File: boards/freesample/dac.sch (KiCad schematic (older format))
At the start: 1 part

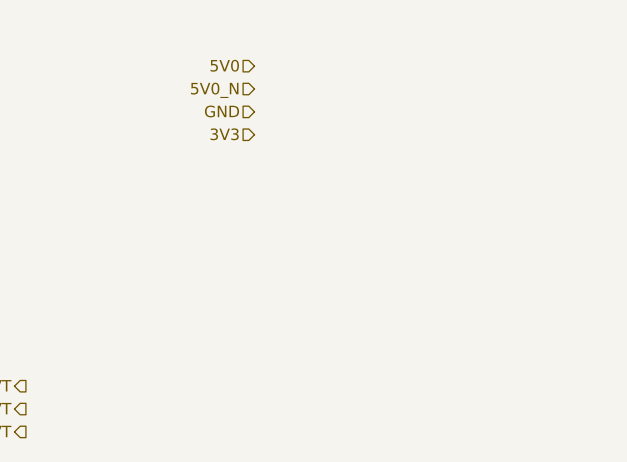
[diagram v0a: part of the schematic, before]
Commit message: Continued initial schematic capture
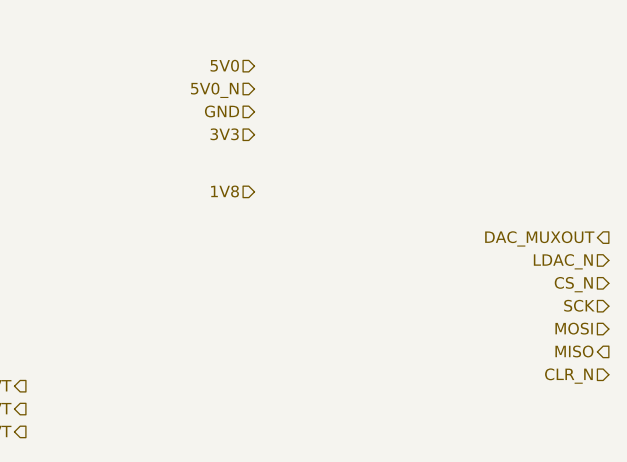
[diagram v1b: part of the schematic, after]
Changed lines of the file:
@@
 $Descr A4 11693 8268
 encoding utf-8
-Sheet 3 11
+Sheet 3 12
 Title "FREESAMPLE Oscilloscope"
-Date "2018-12-15"
+Date "2018-12-17"
 Rev "0.1"
 Comp "Andrew D. Zonenberg / Antikernel Labs"
@@
 Text HLabel 8100 3800 0    50   Input ~ 0
 3V3
+Text HLabel 9650 4250 0    50   Output ~ 0
+DAC_MUXOUT
+Text HLabel 9650 4350 0    50   Input ~ 0
+LDAC_N
+Text HLabel 9650 4450 0    50   Input ~ 0
+CS_N
+Text HLabel 9650 4550 0    50   Input ~ 0
+SCK
+Text HLabel 9650 4650 0    50   Input ~ 0
+MOSI
+Text HLabel 9650 4750 0    50   Output ~ 0
+MISO
+Text HLabel 9650 4850 0    50   Input ~ 0
+CLR_N
+Text HLabel 8100 4050 0    50   Input ~ 0
+1V8
 $EndSCHEMATC

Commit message: Continued work on schematic capture
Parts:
- gave numbers to parts that had none: 1
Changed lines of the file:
@@
 Rev "0.1"
 Comp "Andrew D. Zonenberg / Antikernel Labs"
-Comment1 ""
+Comment1 "DAC for setting sampling point Y position"
 Comment2 ""
 Comment3 ""
@@
 $EndDescr
 $Comp
-L analog-azonenberg:LTC2664 U?
+L analog-azonenberg:LTC2664 U4
 U 1 1 5C15756D
 P 4150 4450
-F 0 "U?" H 4650 7025 50  0000 C CNN
+F 0 "U4" H 4650 7025 50  0000 C CNN
 F 1 "LTC2664" H 4650 6934 50  0000 C CNN
 F 2 "" H 4150 4450 50  0001 C CNN

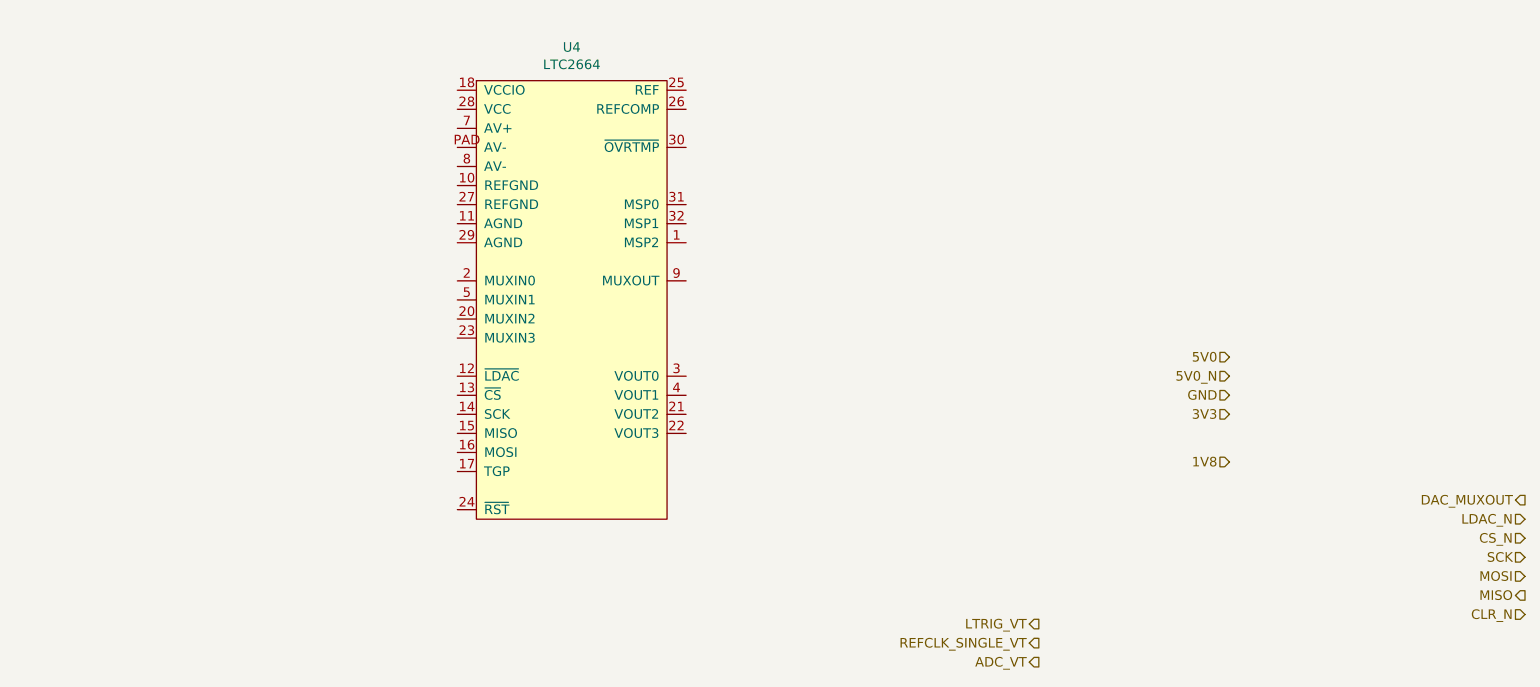
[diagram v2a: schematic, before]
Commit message: Continued work on FREESAMPLE schematic including PSU.
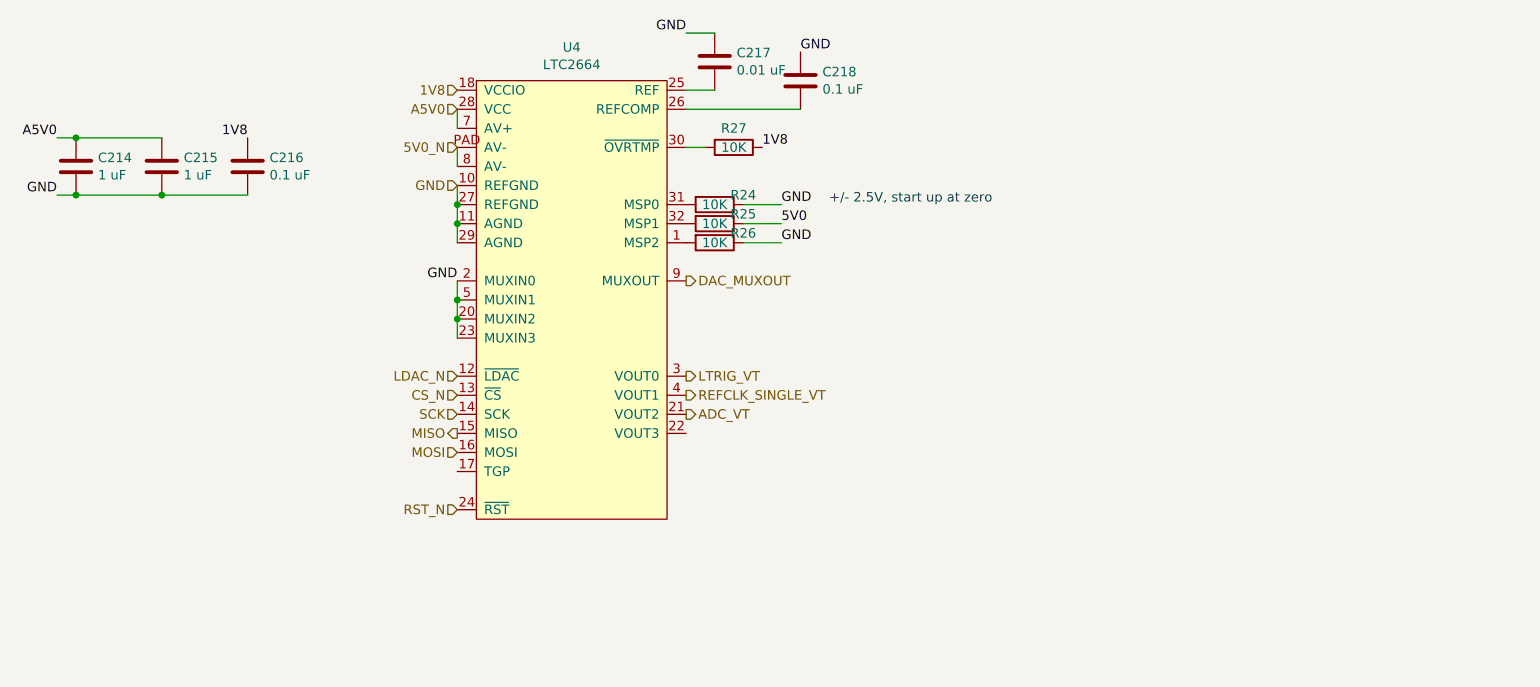
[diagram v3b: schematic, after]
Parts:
- added C214, C215: 1 uF, symbol device:C
- added C216, C218: 0.1 uF, symbol device:C
- added C217: 0.01 uF, symbol device:C
- added R24, R25, R26, R27: 10K, symbol device:R
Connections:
- net 1V8: now also U4.18 (VCCIO), C216.1, R27.1
- net 5V0: now also R25.1
- net 5V0_N: now also U4.8 (AV-), U4.PAD (AV-)
- net ADC_VT: now also U4.21 (VOUT2)
- net CS_N: now also U4.13 (~CS)
- net DAC_MUXOUT: now also U4.9 (MUXOUT)
- net GND: now also U4.10 (REFGND), U4.11 (AGND), U4.2 (MUXIN0), U4.20 (MUXIN2), U4.23 (MUXIN3), U4.27 (REFGND), U4.29 (AGND), U4.5 (MUXIN1), C214.2, C215.2, C216.2, C217.1, C218.1, R24.1, R26.1
- net LDAC_N: now also U4.12 (~LDAC)
- net LTRIG_VT: now also U4.3 (VOUT0)
- net MISO: now also U4.15 (MISO)
- net MOSI: now also U4.16 (MOSI)
- net REFCLK_SINGLE_VT: now also U4.4 (VOUT1)
- net SCK: now also U4.14 (SCK)
- net at U4.1 (MSP2): now also R26.2
- net RST_N: now reaches U4.24 (~RST)
- net at U4.25 (REF): now also C217.2
- net at U4.26 (REFCOMP): now also C218.2
- net A5V0: now reaches U4.28 (VCC)
- net A5V0: now also U4.7 (AV+), C214.1, C215.1
- net at U4.30 (~OVRTMP): now also R27.2
- net at U4.31 (MSP0): now also R24.2
- net at U4.32 (MSP1): now also R25.2
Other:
- note added: "+/- 2.5V, start up at zero"
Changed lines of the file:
@@
 Sheet 3 12
 Title "FREESAMPLE Oscilloscope"
-Date "2018-12-17"
+Date "2019-02-23"
 Rev "0.1"
 Comp "Andrew D. Zonenberg / Antikernel Labs"
@@
 	1    0    0    -1
 $EndComp
-Text HLabel 7100 4900 0    50   Output ~ 0
+Text HLabel 5250 3600 2    50   Output ~ 0
 LTRIG_VT
-Text HLabel 7100 5000 0    50   Output ~ 0
+Text HLabel 5250 3700 2    50   Output ~ 0
 REFCLK_SINGLE_VT
-Text HLabel 7100 5100 0    50   Output ~ 0
+Text HLabel 5250 3800 2    50   Output ~ 0
 ADC_VT
-Text HLabel 8100 3500 0    50   Input ~ 0
+Text HLabel 4050 2200 0    50   Input ~ 0
+A5V0
+Text HLabel 4050 2400 0    50   Input ~ 0
+5V0_N
+Text HLabel 4050 2600 0    50   Input ~ 0
+GND
+Text HLabel 5250 3100 2    50   Output ~ 0
+DAC_MUXOUT
+Text HLabel 4050 3600 0    50   Input ~ 0
+LDAC_N
+Text HLabel 4050 3700 0    50   Input ~ 0
+CS_N
+Text HLabel 4050 3800 0    50   Input ~ 0
+SCK
+Text HLabel 4050 4000 0    50   Input ~ 0
+MOSI
+Text HLabel 4050 3900 0    50   Output ~ 0
+MISO
+Text HLabel 4050 4300 0    50   Input ~ 0
+RST_N
+Text HLabel 4050 2100 0    50   Input ~ 0
+1V8
+Wire Wire Line
+	4050 2200 4050 2300
+Wire Wire Line
+	4050 2400 4050 2500
+Wire Wire Line
+	4050 2600 4050 2700
+Connection ~ 4050 2700
+Wire Wire Line
+	4050 2700 4050 2800
+Connection ~ 4050 2800
+Wire Wire Line
+	4050 2800 4050 2900
+Text Label 4050 3100 2    50   ~ 0
+GND
+Wire Wire Line
+	4050 3100 4050 3200
+Connection ~ 4050 3200
+Wire Wire Line
+	4050 3200 4050 3300
+Connection ~ 4050 3300
+Wire Wire Line
+	4050 3300 4050 3400
+$Comp
+L device:C C214
+U 1 1 5CD2E85E
+P 2050 2500
+F 0 "C214" H 2165 2546 50  0000 L CNN
+F 1 "1 uF" H 2165 2455 50  0000 L CNN
+F 2 "" H 2088 2350 50  0001 C CNN
+F 3 "" H 2050 2500 50  0001 C CNN
+	1    2050 2500
+	1    0    0    -1
+$EndComp
+Text Label 1950 2350 2    50   ~ 0
+A5V0
+Text Label 1950 2650 2    50   ~ 0
+GND
+Wire Wire Line
+	1950 2350 2050 2350
+Wire Wire Line
+	1950 2650 2050 2650
+$Comp
+L device:C C216
+U 1 1 5CD2EFF8
+P 2950 2500
+F 0 "C216" H 3065 2546 50  0000 L CNN
+F 1 "0.1 uF" H 3065 2455 50  0000 L CNN
+F 2 "" H 2988 2350 50  0001 C CNN
+F 3 "" H 2950 2500 50  0001 C CNN
+	1    2950 2500
+	1    0    0    -1
+$EndComp
+Text Label 2950 2350 2    50   ~ 0
+1V8
+Wire Wire Line
+	2050 2650 2500 2650
+Connection ~ 2050 2650
+$Comp
+L device:C C217
+U 1 1 5CD321D9
+P 5400 1950
+F 0 "C217" H 5515 1996 50  0000 L CNN
+F 1 "0.01 uF" H 5515 1905 50  0000 L CNN
+F 2 "" H 5438 1800 50  0001 C CNN
+F 3 "" H 5400 1950 50  0001 C CNN
+	1    5400 1950
+	1    0    0    -1
+$EndComp
+Wire Wire Line
+	5400 2100 5250 2100
+Text Label 5250 1800 2    50   ~ 0
+GND
+Wire Wire Line
+	5250 1800 5400 1800
+$Comp
+L device:C C218
+U 1 1 5CD32B01
+P 5850 2050
+F 0 "C218" H 5965 2096 50  0000 L CNN
+F 1 "0.1 uF" H 5965 2005 50  0000 L CNN
+F 2 "" H 5888 1900 50  0001 C CNN
+F 3 "" H 5850 2050 50  0001 C CNN
+	1    5850 2050
+	1    0    0    -1
+$EndComp
+Wire Wire Line
+	5250 2200 5850 2200
+Text Label 5850 1900 0    50   ~ 0
+GND
+$Comp
+L device:C C215
+U 1 1 5CD336A9
+P 2500 2500
+F 0 "C215" H 2615 2546 50  0000 L CNN
+F 1 "1 uF" H 2615 2455 50  0000 L CNN
+F 2 "" H 2538 2350 50  0001 C CNN
+F 3 "" H 2500 2500 50  0001 C CNN
+	1    2500 2500
+	1    0    0    -1
+$EndComp
+Wire Wire Line
+	2050 2350 2500 2350
+Connection ~ 2050 2350
+Wire Wire Line
+	2500 2650 2950 2650
+Connection ~ 2500 2650
+$Comp
+L device:R R27
+U 1 1 5CD357FE
+P 5500 2400
+F 0 "R27" V 5400 2400 50  0000 C CNN
+F 1 "10K" V 5500 2400 50  0000 C CNN
+F 2 "" V 5430 2400 50  0001 C CNN
+F 3 "" H 5500 2400 50  0001 C CNN
+	1    5500 2400
+	0    1    1    0
+$EndComp
+Wire Wire Line
+	5350 2400 5250 2400
+Text Label 5650 2400 0    50   ~ 0
+1V8
+Text Label 5750 2700 0    50   ~ 0
+GND
+$Comp
+L device:R R24
+U 1 1 5CD379F3
+P 5400 2700
+F 0 "R24" V 5350 2850 50  0000 C CNN
+F 1 "10K" V 5400 2700 50  0000 C CNN
+F 2 "" V 5330 2700 50  0001 C CNN
+F 3 "" H 5400 2700 50  0001 C CNN
+	1    5400 2700
+	0    1    1    0
+$EndComp
+Wire Wire Line
+	5550 2700 5750 2700
+Text Label 5750 2900 0    50   ~ 0
+GND
+$Comp
+L device:R R26
+U 1 1 5CD38388
+P 5400 2900
+F 0 "R26" V 5350 3050 50  0000 C CNN
+F 1 "10K" V 5400 2900 50  0000 C CNN
+F 2 "" V 5330 2900 50  0001 C CNN
+F 3 "" H 5400 2900 50  0001 C CNN
+	1    5400 2900
+	0    1    1    0
+$EndComp
+Wire Wire Line
+	5550 2900 5750 2900
+Text Label 5750 2800 0    50   ~ 0
 5V0
-Text HLabel 8100 3600 0    50   Input ~ 0
-5V0_N
-Text HLabel 8100 3700 0    50   Input ~ 0
-GND
-Text HLabel 8100 3800 0    50   Input ~ 0
-3V3
-Text HLabel 9650 4250 0    50   Output ~ 0
-DAC_MUXOUT
-Text HLabel 9650 4350 0    50   Input ~ 0
-LDAC_N
-Text HLabel 9650 4450 0    50   Input ~ 0
-CS_N
-Text HLabel 9650 4550 0    50   Input ~ 0
-SCK
-Text HLabel 9650 4650 0    50   Input ~ 0
-MOSI
-Text HLabel 9650 4750 0    50   Output ~ 0
-MISO
-Text HLabel 9650 4850 0    50   Input ~ 0
-CLR_N
-Text HLabel 8100 4050 0    50   Input ~ 0
-1V8
+$Comp
+L device:R R25
+U 1 1 5CD38A49
+P 5400 2800
+F 0 "R25" V 5350 2950 50  0000 C CNN
+F 1 "10K" V 5400 2800 50  0000 C CNN
+F 2 "" V 5330 2800 50  0001 C CNN
+F 3 "" H 5400 2800 50  0001 C CNN
+	1    5400 2800
+	0    1    1    0
+$EndComp
+Wire Wire Line
+	5550 2800 5750 2800
+Text Notes 6000 2700 0    50   ~ 0
++/- 2.5V, start up at zero
 $EndSCHEMATC

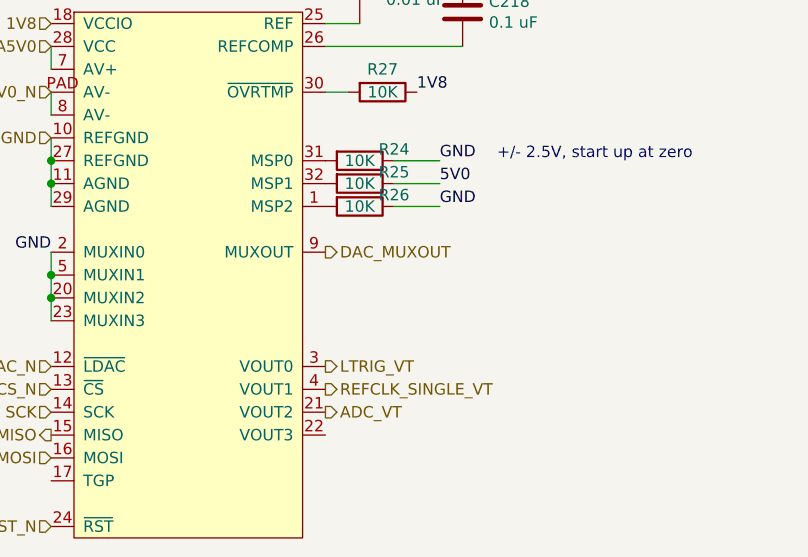
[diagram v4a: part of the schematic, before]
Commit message: Continued schematic capture work. Hooked up most SoM connectors.
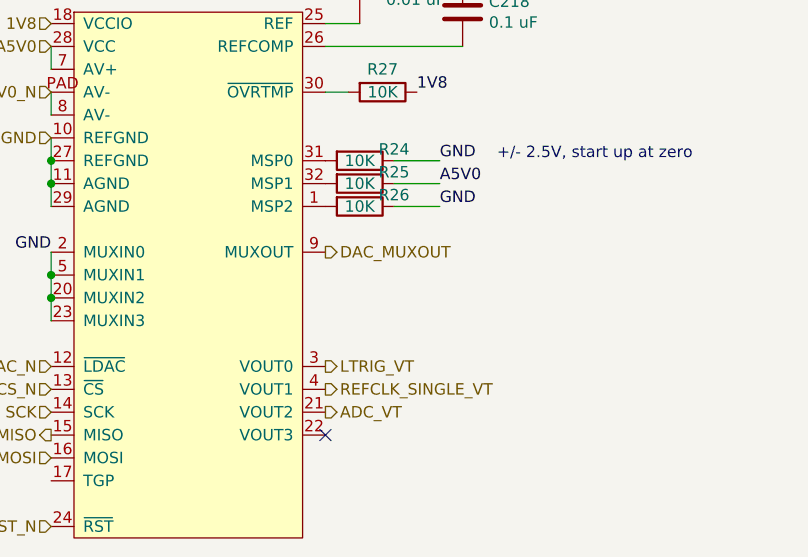
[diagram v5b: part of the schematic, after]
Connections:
- net 5V0 is gone; now on net A5V0: R25.1
- no-connect marks 0 -> 1
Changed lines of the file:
@@
 Sheet 3 12
 Title "FREESAMPLE Oscilloscope"
-Date "2019-02-26"
+Date "2019-03-10"
 Rev "0.1"
 Comp "Andrew D. Zonenberg / Antikernel Labs"
 Comment1 "DAC for setting sampling point Y position"
-Comment2 ""
+Comment2 "Ready for review"
 Comment3 ""
 Comment4 ""
@@
 	5550 2900 5750 2900
 Text Label 5750 2800 0    50   ~ 0
-5V0
+A5V0
 $Comp
 L device:R R25
@@
 Text Notes 6000 2700 0    50   ~ 0
 +/- 2.5V, start up at zero
+NoConn ~ 5250 3900
 $EndSCHEMATC

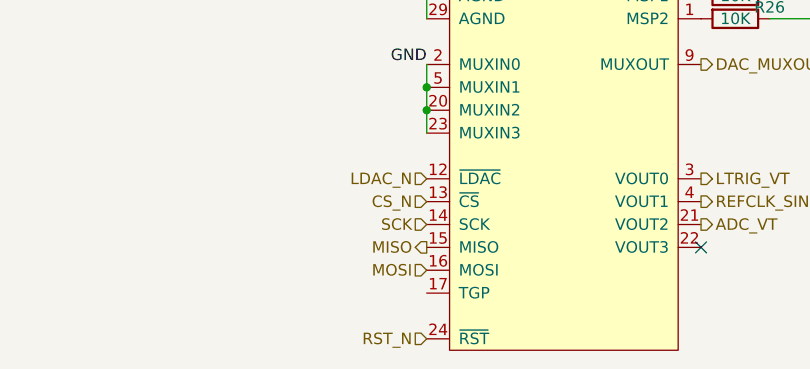
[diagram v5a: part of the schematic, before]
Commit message: Lots of ERC fixes, added CML-to-LVDS buffers for FPGA input signals
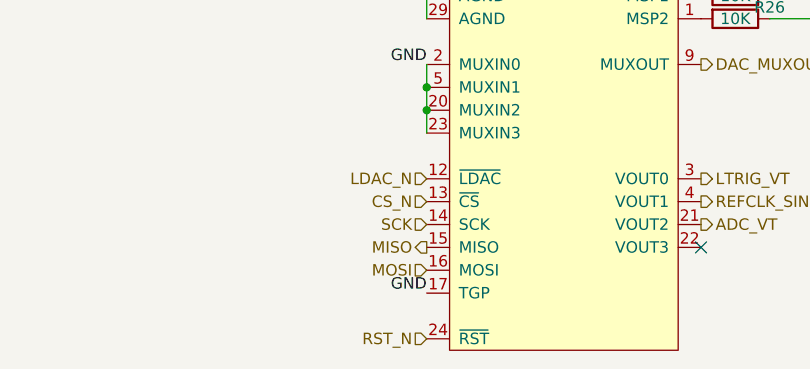
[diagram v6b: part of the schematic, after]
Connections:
- net GND: now also U4.17 (TGP)
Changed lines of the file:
@@
 +/- 2.5V, start up at zero
 NoConn ~ 5250 3900
+Text Label 4050 4100 2    50   ~ 0
+GND
 $EndSCHEMATC
